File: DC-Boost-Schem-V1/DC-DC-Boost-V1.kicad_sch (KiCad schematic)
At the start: 0 parts

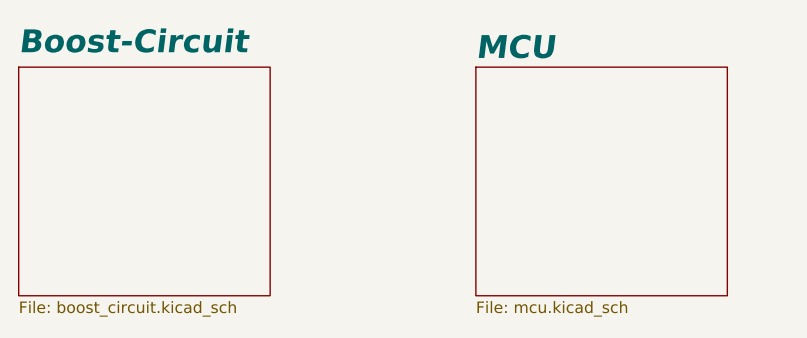
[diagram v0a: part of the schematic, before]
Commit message: Added OLED Screen, adjusted parameters on efuses and op-amp IC
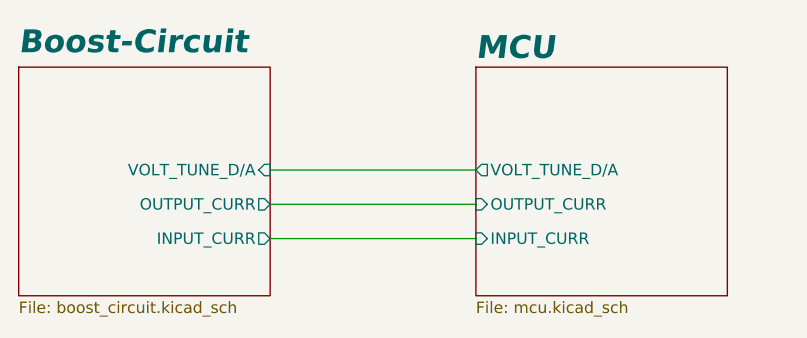
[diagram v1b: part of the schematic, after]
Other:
- sheet Boost-Circuit ports: added INPUT_CURR, OUTPUT_CURR, VOLT_TUNE_D/A; removed none
- sheet MCU ports: added INPUT_CURR, OUTPUT_CURR, VOLT_TUNE_D/A; removed none
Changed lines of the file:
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@@
 		(comment 1 "Designed by: Nicholas semmens")
+	)
+	(wire
+		(pts
+			(xy 53.34 44.45) (xy 76.2 44.45)
+		)
+		(stroke
+			(width 0)
+			(type default)
+		)
+	)
+	(wire
+		(pts
+			(xy 53.34 40.64) (xy 76.2 40.64)
+		)
+		(stroke
+			(width 0)
+			(type default)
+		)
+	)
+	(wire
+		(pts
+			(xy 53.34 36.83) (xy 76.2 36.83)
+		)
+		(stroke
+			(width 0)
+			(type default)
+		)
 	)
 	(sheet
@@
 			)
 		)
+		(pin "VOLT_TUNE_D{slash}A" output
+			(at 76.2 36.83 180)
+			(effects
+				(font
+					(size 1.27 1.27)
+				)
+				(justify left)
+			)
+		)
+		(pin "INPUT_CURR" input
+			(at 76.2 44.45 180)
+			(effects
+				(font
+					(size 1.27 1.27)
+				)
+				(justify left)
+			)
+		)
+		(pin "OUTPUT_CURR" input
+			(at 76.2 40.64 180)
+			(effects
+				(font
+					(size 1.27 1.27)
+				)
+				(justify left)
+			)
+		)
 		(instances
 			(project "DC-DC-Boost-V1"
@@
 			)
 		)
+		(pin "VOLT_TUNE_D{slash}A" input
+			(at 53.34 36.83 0)
+			(effects
+				(font
+					(size 1.27 1.27)
+				)
+				(justify right)
+			)
+		)
+		(pin "INPUT_CURR" output
+			(at 53.34 44.45 0)
+			(effects
+				(font
+					(size 1.27 1.27)
+				)
+				(justify right)
+			)
+		)
+		(pin "OUTPUT_CURR" output
+			(at 53.34 40.64 0)
+			(effects
+				(font
+					(size 1.27 1.27)
+				)
+				(justify right)
+			)
+		)

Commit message: Updated Layout
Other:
- sheet MCU renamed MCU+POWER+CAN
- removed sheet Connections
- added sheet TRK Pin Isolation (TRK_PIN_ISO_sch.kicad_sch)
- added sheet Voltage Sensing Input Terminal (connections.kicad_sch)
- added sheet Voltage Sensing Output Terminal (voltage_output.kicad_sch)
- sheet Boost-Circuit ports: added TRK, VOLT_IN_1, VOLT_IN_2; removed VOLT_TUNE_D/A
- sheet MCU+POWER+CAN ports: added ISO_VOLT_INPUT_TERMINAL, ISO_VOLT_OUTPUT_TERMINAL; removed none

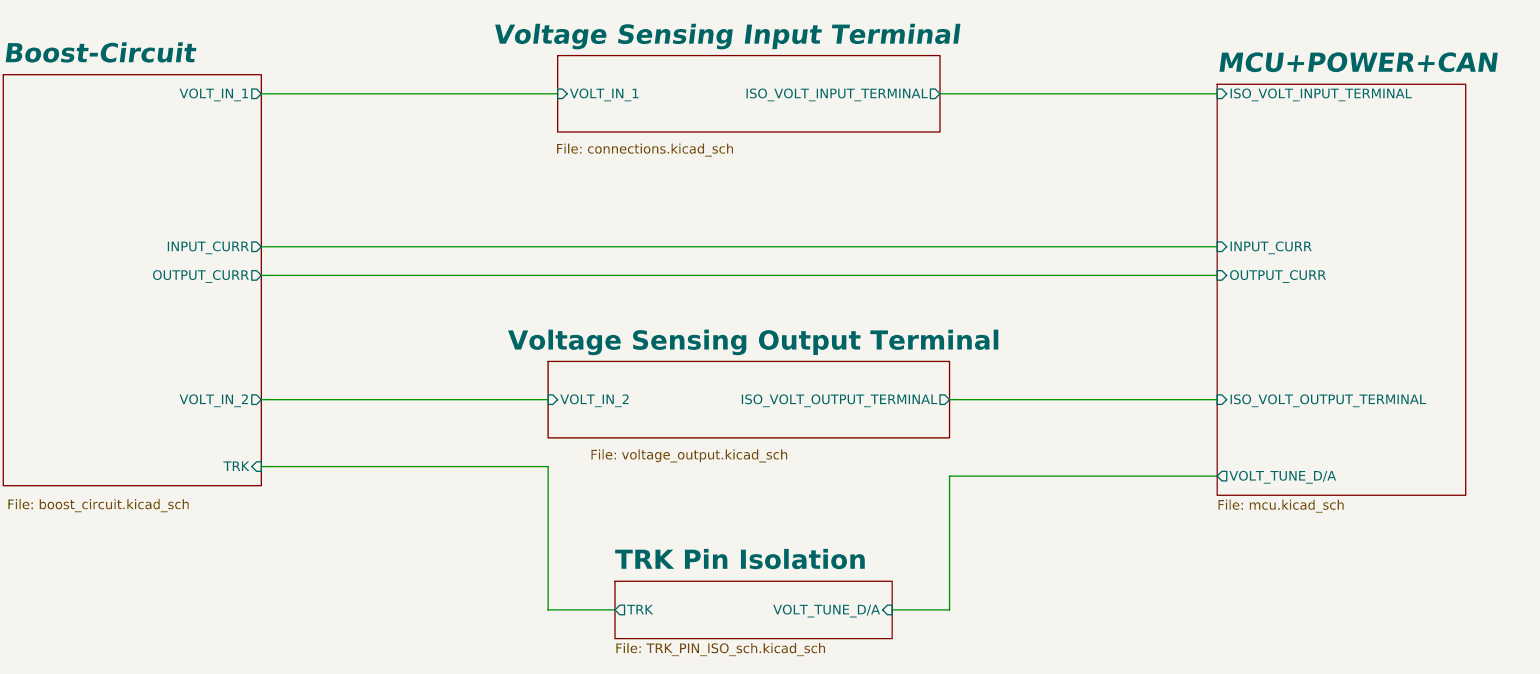
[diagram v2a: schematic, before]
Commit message: Added efuse model
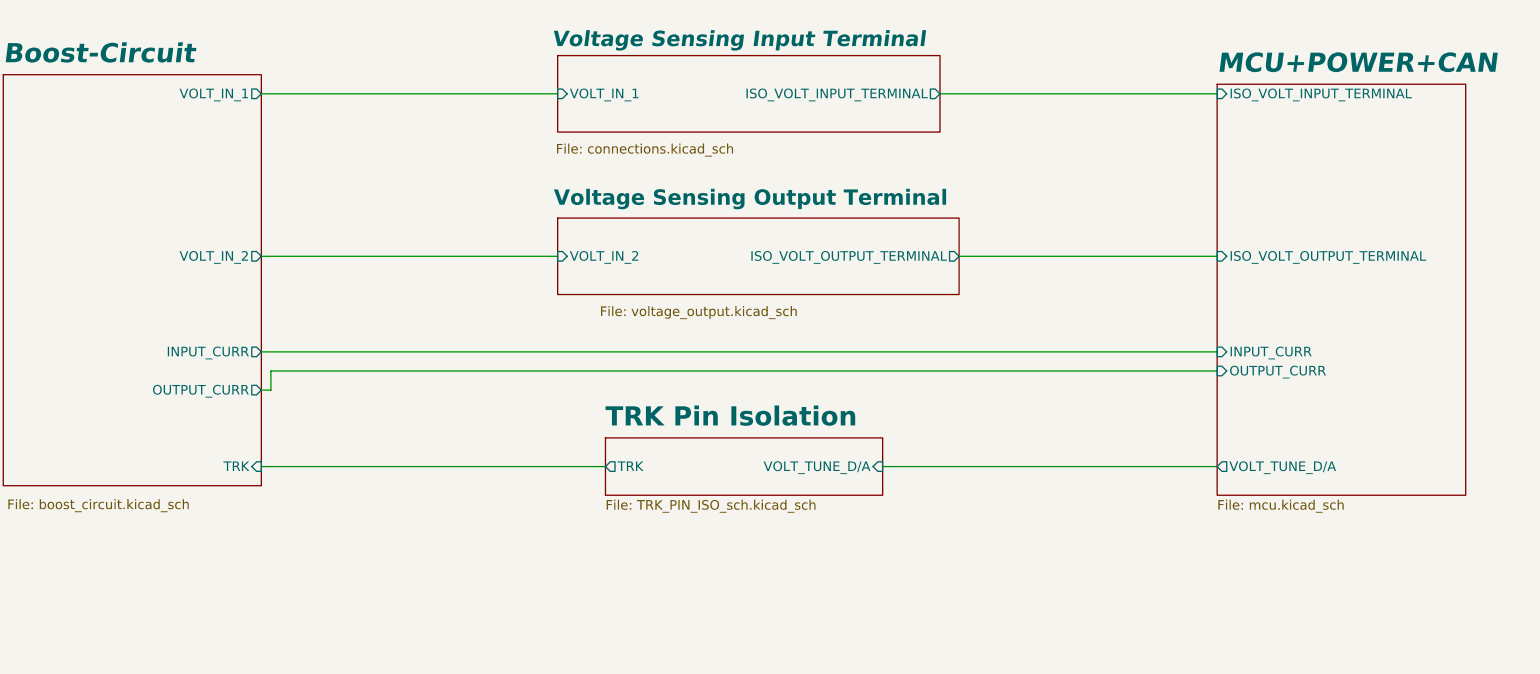
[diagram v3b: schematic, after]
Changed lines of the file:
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@@
 	(wire
 		(pts
-			(xy 78.74 81.28) (xy 205.74 81.28)
-		)
-		(stroke
-			(width 0)
-			(type default)
-		)
-	)
-	(wire
-		(pts
-			(xy 170.18 129.54) (xy 162.56 129.54)
+			(xy 78.74 95.25) (xy 205.74 95.25)
+		)
+		(stroke
+			(width 0)
+			(type default)
+		)
+	)
+	(wire
+		(pts
+			(xy 161.29 110.49) (xy 205.74 110.49)
+		)
+		(stroke
+			(width 0)
+			(type default)
+		)
+	)
+	(wire
+		(pts
+			(xy 171.45 82.55) (xy 205.74 82.55)
 		)
 		(stroke
@@
 	(wire
 		(pts
-			(xy 170.18 111.76) (xy 170.18 129.54)
-		)
-		(stroke
-			(width 0)
-			(type default)
-		)
-	)
-	(wire
-		(pts
-			(xy 205.74 111.76) (xy 170.18 111.76)
-		)
-		(stroke
-			(width 0)
-			(type default)
-		)
-	)
-	(wire
-		(pts
-			(xy 116.84 129.54) (xy 116.84 110.49)
-		)
-		(stroke
-			(width 0)
-			(type default)
-		)
-	)
-	(wire
-		(pts
-			(xy 125.73 129.54) (xy 116.84 129.54)
-		)
-		(stroke
-			(width 0)
-			(type default)
-		)
-	)
-	(wire
-		(pts
-			(xy 116.84 110.49) (xy 78.74 110.49)
-		)
-		(stroke
-			(width 0)
-			(type default)
-		)
-	)
-	(wire
-		(pts
-			(xy 170.18 101.6) (xy 205.74 101.6)
-		)
-		(stroke
-			(width 0)
-			(type default)
-		)
-	)
-	(wire
-		(pts
-			(xy 78.74 101.6) (xy 116.84 101.6)
-		)
-		(stroke
-			(width 0)
-			(type default)
-		)
-	)
-	(wire
-		(pts
-			(xy 78.74 85.09) (xy 205.74 85.09)
+			(xy 80.01 100.33) (xy 80.01 97.79)
+		)
+		(stroke
+			(width 0)
+			(type default)
+		)
+	)
+	(wire
+		(pts
+			(xy 78.74 110.49) (xy 124.46 110.49)
+		)
+		(stroke
+			(width 0)
+			(type default)
+		)
+	)
+	(wire
+		(pts
+			(xy 78.74 100.33) (xy 80.01 100.33)
+		)
+		(stroke
+			(width 0)
+			(type default)
+		)
+	)
+	(wire
+		(pts
+			(xy 80.01 97.79) (xy 205.74 97.79)
+		)
+		(stroke
+			(width 0)
+			(type default)
+		)
+	)
+	(wire
+		(pts
+			(xy 78.74 82.55) (xy 118.11 82.55)
 		)
 		(stroke
@@
 		)
 		(pin "VOLT_TUNE_D{slash}A" output
-			(at 205.74 111.76 180)
+			(at 205.74 110.49 180)
 			(effects
 				(font
@@
 		)
 		(pin "INPUT_CURR" input
-			(at 205.74 81.28 180)
+			(at 205.74 95.25 180)
 			(effects
 				(font
@@
 		)
 		(pin "OUTPUT_CURR" input
-			(at 205.74 85.09 180)
+			(at 205.74 97.79 180)
 			(effects
 				(font
@@
 		)
 		(pin "ISO_VOLT_OUTPUT_TERMINAL" input
-			(at 205.74 101.6 180)
+			(at 205.74 82.55 180)
 			(effects
 				(font
@@
 	)
 	(sheet
-		(at 116.84 96.52)
+		(at 118.11 77.47)
 		(size 53.34 10.16)
 		(stroke
@@
 		)
 		(property "Sheetname" "Voltage Sensing Output Terminal"
-			(at 111.506 95.25 0)
-			(effects
-				(font
-					(size 2.54 2.54)
+			(at 117.602 75.946 0)
+			(effects
+				(font
+					(size 2.032 2.032)
 					(bold yes)
 				)
@@
 		)
 		(property "Sheetfile" "voltage_output.kicad_sch"
-			(at 122.428 108.204 0)
+			(at 123.698 89.154 0)
 			(effects
 				(font
@@
 		)
 		(pin "ISO_VOLT_OUTPUT_TERMINAL" output
-			(at 170.18 101.6 0)
+			(at 171.45 82.55 0)
 			(effects
 				(font
@@
 		)
 		(pin "VOLT_IN_2" input
-			(at 116.84 101.6 180)
+			(at 118.11 82.55 180)
 			(effects
 				(font
@@
 	)
 	(sheet
-		(at 125.73 125.73)
+		(at 124.46 106.68)
 		(size 36.83 7.62)
 		(fields_autoplaced yes)
@@
 		)
 		(property "Sheetname" "TRK Pin Isolation"
-			(at 125.73 124.3834 0)
+			(at 124.46 105.3334 0)
 			(effects
 				(font
@@
 		)
 		(property "Sheetfile" "TRK_PIN_ISO_sch.kicad_sch"
-			(at 125.73 133.9346 0)
+			(at 124.46 114.8846 0)
 			(effects
 				(font
@@
 		)
 		(pin "TRK" output
-			(at 125.73 129.54 180)
+			(at 124.46 110.49 180)
 			(effects
 				(font
@@
 		)
 		(pin "VOLT_TUNE_D{slash}A" input
-			(at 162.56 129.54 0)
+			(at 161.29 110.49 0)
 			(effects
 				(font
@@
 		)
 		(property "Sheetname" "Voltage Sensing Input Terminal"
-			(at 109.474 54.61 0)
-			(effects
-				(font
-					(size 2.54 2.54)
+			(at 117.348 54.864 0)
+			(effects
+				(font
+					(size 2.032 2.032)
 					(bold yes)
 					(italic yes)
@@
 		)
 		(pin "INPUT_CURR" output
-			(at 78.74 81.28 0)
+			(at 78.74 95.25 0)
 			(effects
 				(font
@@
 		)
 		(pin "OUTPUT_CURR" output
-			(at 78.74 85.09 0)
+			(at 78.74 100.33 0)
 			(effects
 				(font
@@
 		)
 		(pin "VOLT_IN_2" output
-			(at 78.74 101.6 0)
-			(effects
-				(font
+			(at 78.74 82.55 0)
+			(effects
+				(font

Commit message: Worked on layout
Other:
- note added: "Fix grounds, make uupside down U for gndref place votlasge sensors"
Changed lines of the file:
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@@
-	(wire
-		(pts
-			(xy 80.01 100.33) (xy 80.01 97.79)
-		)
-		(stroke
-			(width 0)
-			(type default)
-		)
-	)
 	(wire
 		(pts
@@
 	(wire
 		(pts
-			(xy 78.74 100.33) (xy 80.01 100.33)
-		)
-		(stroke
-			(width 0)
-			(type default)
-		)
-	)
-	(wire
-		(pts
-			(xy 80.01 97.79) (xy 205.74 97.79)
+			(xy 78.74 100.33) (xy 205.74 100.33)
 		)
 		(stroke
@@
 			(width 0)
 			(type default)
+		)
+	)
+	(text "Fix grounds, make uupside down U for gndref\nplace votlasge sensors\n\n\n"
+		(exclude_from_sim no)
+		(at 58.42 153.035 0)
+		(effects
+			(font
+				(size 1.27 1.27)
+			)
 		)
 	)
@@
 		)
 		(pin "OUTPUT_CURR" input
-			(at 205.74 97.79 180)
+			(at 205.74 100.33 180)
 			(effects
 				(font

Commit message: worked on layout
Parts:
- added H5, H6, H7, H8: MountingHole, MountingHole:MountingHole_3.5mm, symbol Mechanical:MountingHole

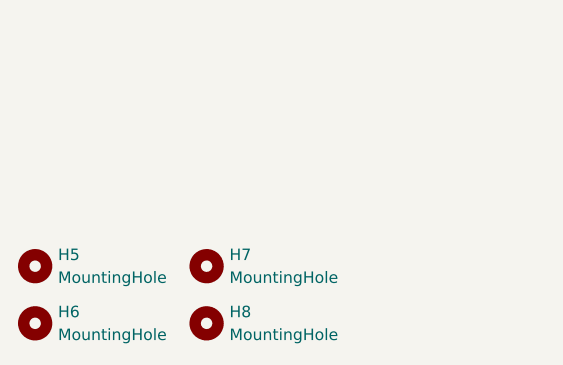
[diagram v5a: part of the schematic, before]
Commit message: More layout and routing
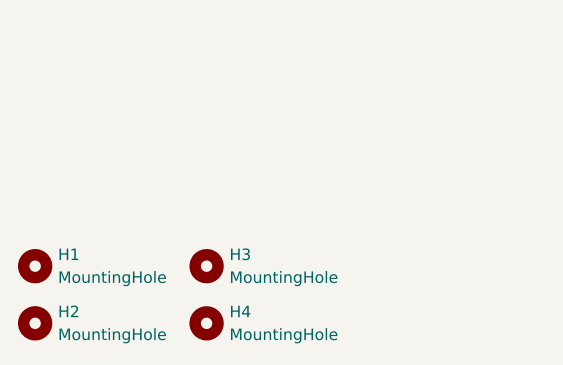
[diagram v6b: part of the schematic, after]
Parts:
- renumbered H5 to H1, H6 to H2, H7 to H3, H8 to H4
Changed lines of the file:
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@@
 		(dnp no)
 		(fields_autoplaced yes)
-		(property "Reference" "H7"
+		(property "Reference" "H3"
 			(at 40.005 184.1499 0)
 			(effects
@@
 			(project "DC-DC-Boost-V1"
 				(path "/892bc44b-f7f8-4677-bf53-06d5523b6450"
-					(reference "H7")
+					(reference "H3")
 					(unit 1)
 				)
@@
 		(dnp no)
 		(fields_autoplaced yes)
-		(property "Reference" "H6"
+		(property "Reference" "H2"
 			(at 20.955 190.4999 0)
 			(effects
@@
 			(project "DC-DC-Boost-V1"
 				(path "/892bc44b-f7f8-4677-bf53-06d5523b6450"
-					(reference "H6")
+					(reference "H2")
 					(unit 1)
 				)
@@
 		(dnp no)
 		(fields_autoplaced yes)
-		(property "Reference" "H8"
+		(property "Reference" "H4"
 			(at 40.005 190.4999 0)
 			(effects
@@
 			(project "DC-DC-Boost-V1"
 				(path "/892bc44b-f7f8-4677-bf53-06d5523b6450"
-					(reference "H8")
+					(reference "H4")
 					(unit 1)
 				)
@@
 		(dnp no)
 		(fields_autoplaced yes)
-		(property "Reference" "H5"
+		(property "Reference" "H1"
 			(at 20.955 184.1499 0)
 			(effects
@@
 			(project "DC-DC-Boost-V1"
 				(path "/892bc44b-f7f8-4677-bf53-06d5523b6450"
-					(reference "H5")
-					(unit 1)
-				)
+					(reference "H1")
+					(unit 1)
+				)
